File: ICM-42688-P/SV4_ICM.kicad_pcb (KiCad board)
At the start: 2 copper layers, 17.8 x 26.4 mm, 19 parts, among them U1 SuperMini nRF52840, U2 ICM-42688-P, U3 MMC5983MA

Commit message: - Changed PCB "mirror" to 1mm NPTH, LED will shine through hole rather than   reflect to side.
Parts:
- added REF**: 1mm npth, justPads_custom:1mm npth, F.Cu at (136.1, 81.3)
- added REF**: 1mm npth, justPads_custom:1mm npth, F.Cu at (151.4, 81.3)
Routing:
- net GND: track 23.0 -> 24.7 mm

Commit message: Added supermini debug jig. Moved case button location to match PCB.
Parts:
- REF** (x2): value 1mm npth -> 1-1.25; footprint justPads_custom:1mm npth -> justPads_custom:1-1.25
- TP1, TP2: footprint justPads_custom:3_4-2.5_3.5 -> justPads_custom:2_4-1.5_3.5_1

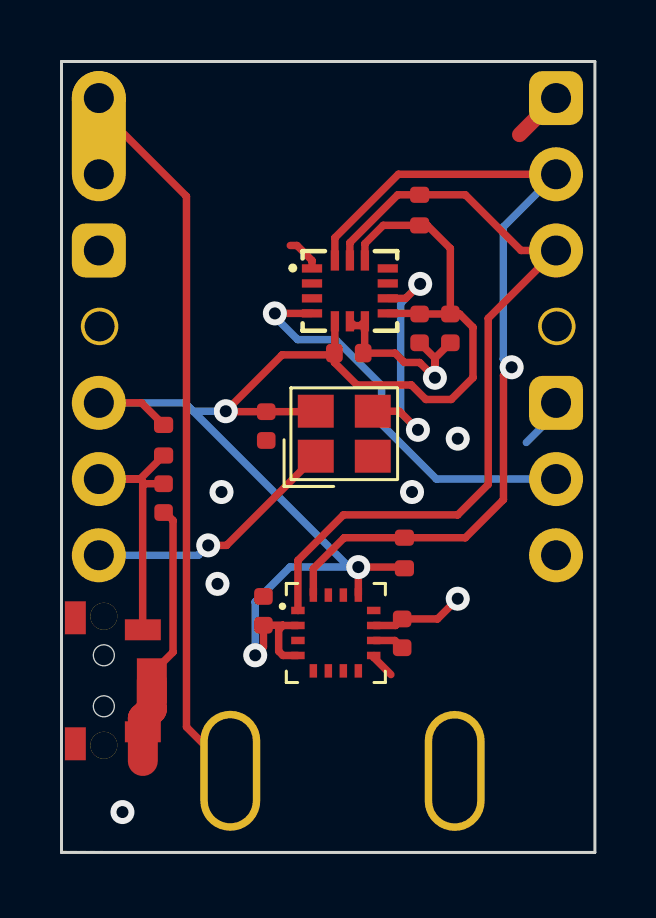
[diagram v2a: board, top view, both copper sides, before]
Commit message: - Added dimensions to dock pcb - some other stuff probably that i forgot to write down
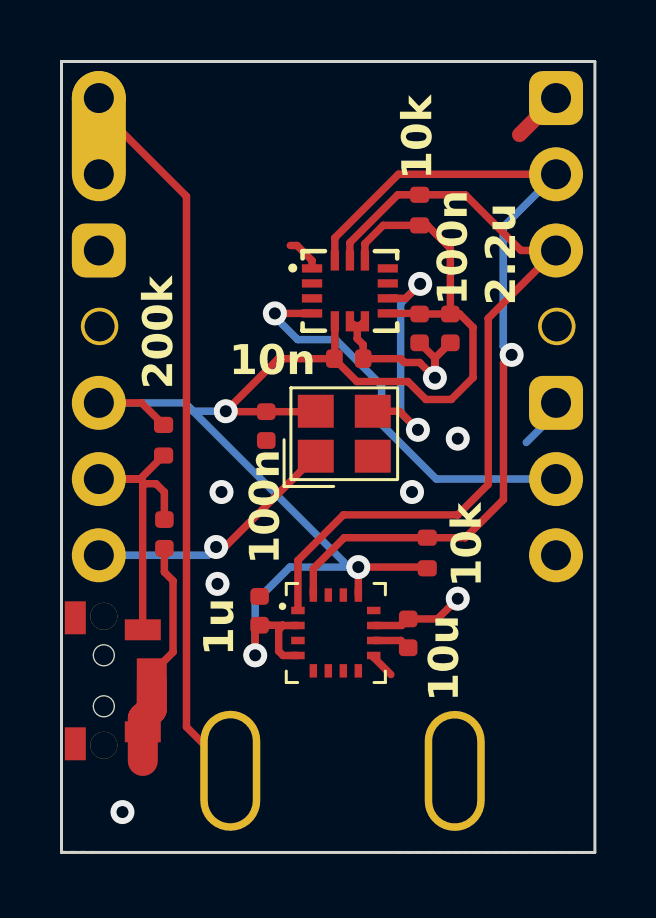
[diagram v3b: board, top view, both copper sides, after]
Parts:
- moved C1 1.19 mm to (138.3, 88.3)
- moved R2 0.76 mm to (147.1, 88.9)
- moved C5 0.20 mm to (146.4, 91.6)
- moved C3 0.18 mm to (144.4, 82.4)
- moved C2 0.13 mm to (141.5, 90.8)
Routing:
- net +3V3: track 52.2 -> 53.3 mm
- net Net-(U1-P0.31-LF): track 9.60 -> 10.7 mm
- net GND: track 24.7 -> 23.8 mm
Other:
- board text added: "100n"
- board text added: "100n 2.2u"
- board text added: "10k"
- board text added: "10n"
- board text added: "10u"
- board text added: "1u"
- board text added: "200k"

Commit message: - Added battery disconnect switch on PCB - Fixed dock dimension issues - Removed stl files from dock folder. Just split the step file in your slicer. - Added 3mf file for dock models. Compatible with Orca Slicer.
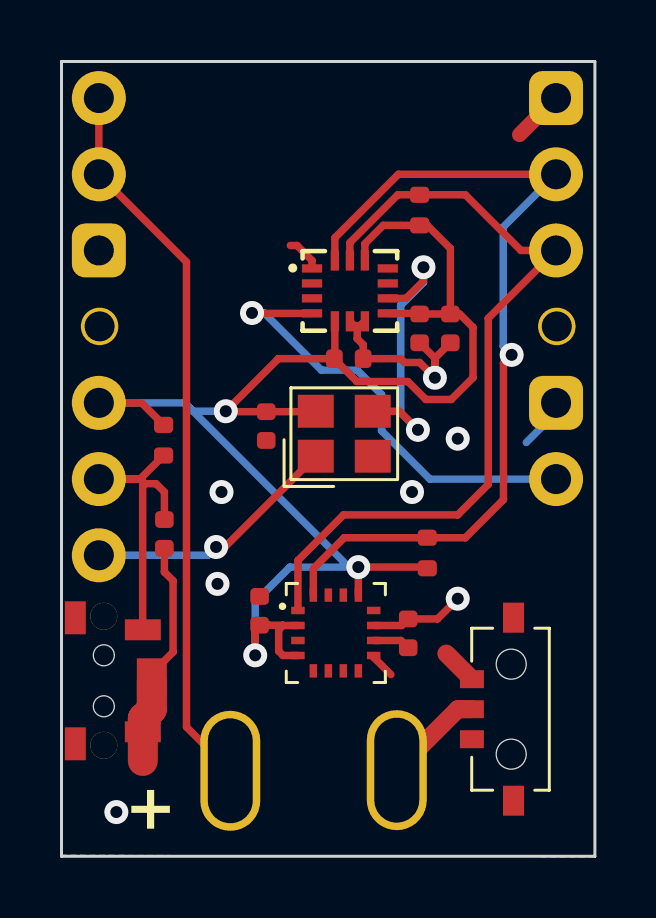
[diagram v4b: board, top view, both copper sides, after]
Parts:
- added U4: K3-1295S-E1, buttons_custom:K3-1295S-E1, F.Cu at (149.2, 94.1)
- C1: value 10uF -> 100nF
- moved TP2 1.93 mm to (146.1, 96.1)
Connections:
- TP2 pad 1: GND -> Net-(TP2-Pad1)
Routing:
- net Net-(TP2-Pad1): track 0.00 -> 3.35 mm
- net INT1: track 14.2 -> 15.6 mm
- net GND: track 23.8 -> 25.1 mm
- net Net-(U2-INT2/FSYNC/CLKIN): track 8.41 -> 9.62 mm
- net unconnected-(U1-P0.20-Pad6): track 0.57 -> 0.00 mm
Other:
- board size 17.8 x 26.4 mm -> 17.8 x 26.5 mm
- board text added: "+"
- board text added: "MP-S-4.4.1"
- board text added: "X"
- board text removed: "100n"
- board text removed: "100n 2.2u"
- board text removed: "10k"
- board text removed: "10n"
- board text removed: "10u"
- board text removed: "1u"
- board text removed: "200k"
